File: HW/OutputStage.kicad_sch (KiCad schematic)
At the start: 10 parts, among them U1 DRV8244S-Q1, U2 DRV8244S-Q1

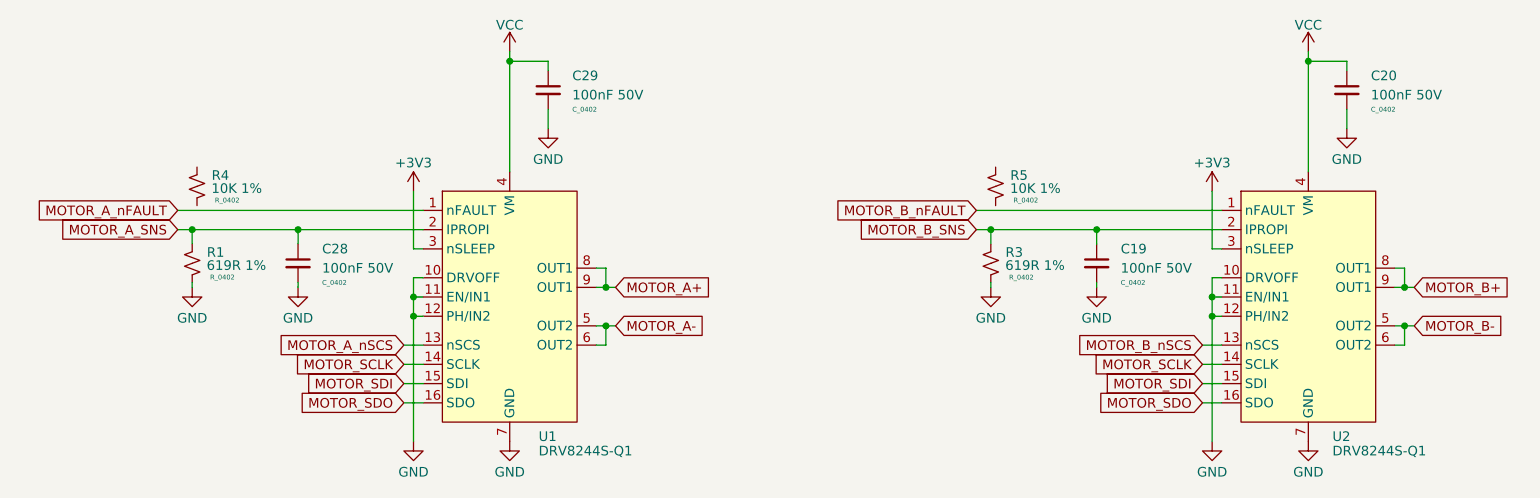
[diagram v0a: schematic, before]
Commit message: WIP - Layout XT30/PCB Finger Positions
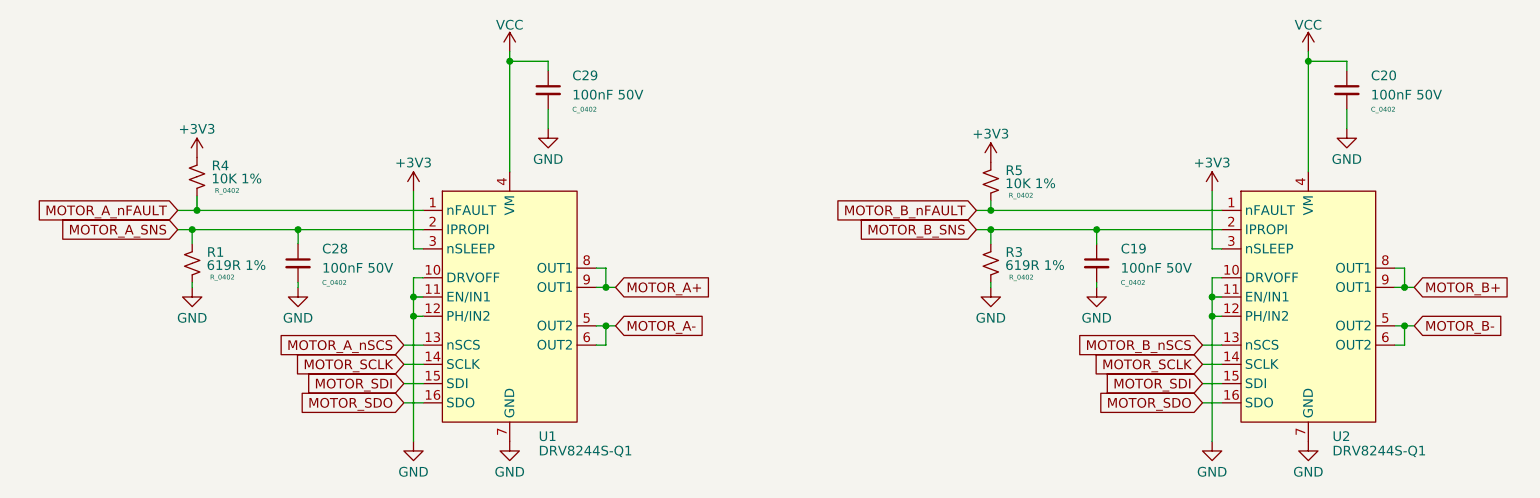
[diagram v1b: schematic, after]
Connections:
- net +3V3: now also R4.1, R5.1
- net MOTOR_A_nFAULT: now also R4.2
- net MOTOR_B_nFAULT: now also R5.2
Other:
- title: WEKA ESC - 20A -> KAKAPO ESC - 20A
- moved on the sheet: R4, R5

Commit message: WIP - Layout Motor Drivers + Buck Circuit
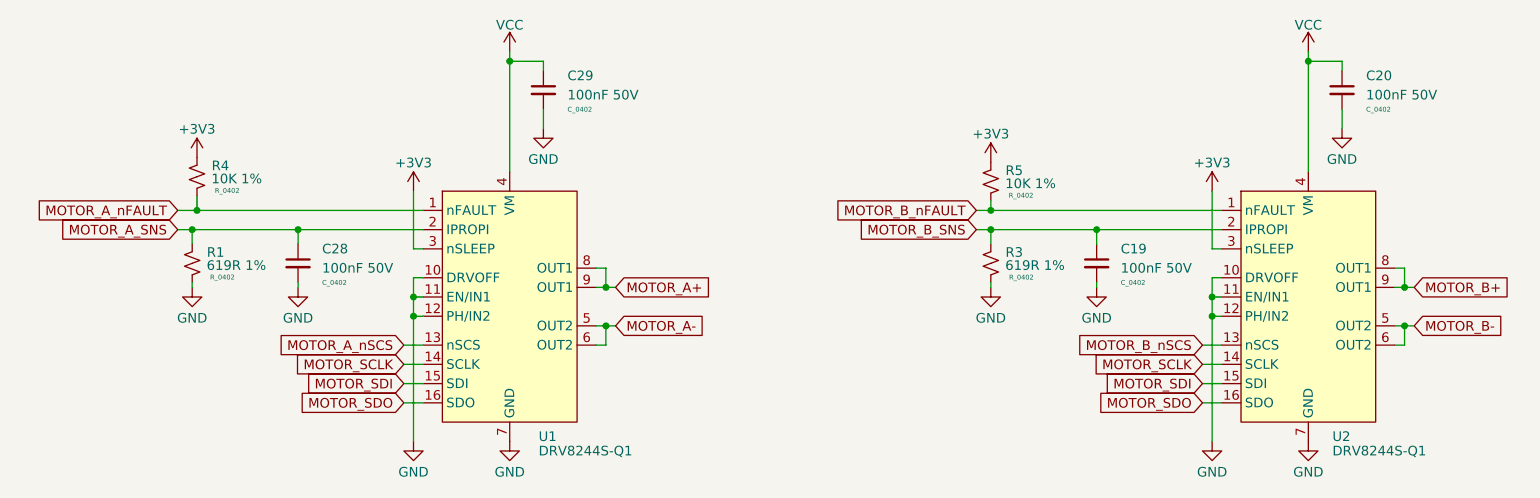
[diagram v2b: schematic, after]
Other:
- moved on the sheet: C20, C29
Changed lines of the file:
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@@
+    (stroke (width 0) (type default))
+  )
+  (wire (pts (xy 109.855 69.85) (xy 114.3 69.85))
     (stroke (width 0) (type default))
   )
@@
     (stroke (width 0) (type default))
   )
-  (wire (pts (xy 114.935 71.12) (xy 114.935 69.85))
+  (wire (pts (xy 114.3 71.12) (xy 114.3 69.85))
     (stroke (width 0) (type default))
   )
@@
     (stroke (width 0) (type default))
   )
-  (wire (pts (xy 220.345 71.12) (xy 220.345 69.85))
+  (wire (pts (xy 219.71 71.12) (xy 219.71 69.85))
     (stroke (width 0) (type default))
   )
@@
     (stroke (width 0) (type default))
   )
-  (wire (pts (xy 109.855 69.85) (xy 114.935 69.85))
-    (stroke (width 0) (type default))
-  )
   (wire (pts (xy 98.425 98.425) (xy 97.155 98.425))
     (stroke (width 0) (type default))
@@
     (stroke (width 0) (type default))
   )
+  (wire (pts (xy 219.71 76.2) (xy 219.71 78.74))
+    (stroke (width 0) (type default))
+  )
   (wire (pts (xy 109.855 69.85) (xy 109.855 84.455))
     (stroke (width 0) (type default))
@@
     (stroke (width 0) (type default))
   )
-  (wire (pts (xy 220.345 76.2) (xy 220.345 78.74))
-    (stroke (width 0) (type default))
-  )
   (wire (pts (xy 67.945 99.695) (xy 67.945 99.06))
     (stroke (width 0) (type default))
@@
     (stroke (width 0) (type default))
   )
-  (wire (pts (xy 114.935 76.2) (xy 114.935 78.74))
+  (wire (pts (xy 114.3 76.2) (xy 114.3 78.74))
     (stroke (width 0) (type default))
   )
@@
     (stroke (width 0) (type default))
   )
-  (wire (pts (xy 215.265 69.85) (xy 220.345 69.85))
+  (wire (pts (xy 215.265 69.85) (xy 219.71 69.85))
     (stroke (width 0) (type default))
   )
@@
     )
   )
-  (symbol (lib_id "power:GND") (at 114.935 78.74 0) (unit 1)
+  (symbol (lib_id "power:GND") (at 114.3 78.74 0) (unit 1)
     (in_bom yes) (on_board yes) (dnp no)
-    (property "Reference" "#PWR026" (at 114.935 85.09 0)
-      (effects (font (size 1.27 1.27)) hide)
-    )
-    (property "Value" "GND" (at 114.935 82.804 0)
+    (property "Reference" "#PWR026" (at 114.3 85.09 0)
+      (effects (font (size 1.27 1.27)) hide)
+    )
+    (property "Value" "GND" (at 114.3 82.804 0)
       (effects (font (size 1.27 1.27)))
     )
-    (property "Footprint" "" (at 114.935 78.74 0)
-      (effects (font (size 1.27 1.27)) hide)
-    )
-    (property "Datasheet" "" (at 114.935 78.74 0)
+    (property "Footprint" "" (at 114.3 78.74 0)
+      (effects (font (size 1.27 1.27)) hide)
+    )
+    (property "Datasheet" "" (at 114.3 78.74 0)
       (effects (font (size 1.27 1.27)) hide)
     )
@@
     )
   )
-  (symbol (lib_id "power:GND") (at 220.345 78.74 0) (unit 1)
+  (symbol (lib_id "power:GND") (at 219.71 78.74 0) (unit 1)
     (in_bom yes) (on_board yes) (dnp no)
-    (property "Reference" "#PWR028" (at 220.345 85.09 0)
-      (effects (font (size 1.27 1.27)) hide)
-    )
-    (property "Value" "GND" (at 220.345 82.804 0)
+    (property "Reference" "#PWR028" (at 219.71 85.09 0)
+      (effects (font (size 1.27 1.27)) hide)
+    )
+    (property "Value" "GND" (at 219.71 82.804 0)
       (effects (font (size 1.27 1.27)))
     )
-    (property "Footprint" "" (at 220.345 78.74 0)
-      (effects (font (size 1.27 1.27)) hide)
-    )
-    (property "Datasheet" "" (at 220.345 78.74 0)
+    (property "Footprint" "" (at 219.71 78.74 0)
+      (effects (font (size 1.27 1.27)) hide)
+    )
+    (property "Datasheet" "" (at 219.71 78.74 0)
       (effects (font (size 1.27 1.27)) hide)
     )
@@
     )
   )
-  (symbol (lib_id "C_Capacitor:C_0402") (at 114.935 73.66 0) (unit 1)
+  (symbol (lib_id "C_Capacitor:C_0402") (at 114.3 73.66 0) (unit 1)
     (in_bom yes) (on_board yes) (dnp no) (fields_autoplaced)
-    (property "Reference" "C29" (at 118.11 71.7613 0)
+    (property "Reference" "C29" (at 117.475 71.7613 0)
       (effects (font (size 1.27 1.27)) (justify left))
     )
-    (property "Value" "100nF 50V" (at 118.11 74.3013 0)
+    (property "Value" "100nF 50V" (at 117.475 74.3013 0)
       (effects (font (size 1.27 1.27)) (justify left))
     )
-    (property "Footprint" "C_Capacitor:C_0402" (at 111.76 73.66 90)
-      (effects (font (size 1.27 1.27)) hide)
-    )
-    (property "Datasheet" "" (at 117.475 71.12 0)
-      (effects (font (size 1.27 1.27)) hide)
-    )
-    (property "Size" "C_0402" (at 118.11 76.2063 0)
+    (property "Footprint" "C_Capacitor:C_0402" (at 111.125 73.66 90)
+      (effects (font (size 1.27 1.27)) hide)
+    )
+    (property "Datasheet" "" (at 116.84 71.12 0)
+      (effects (font (size 1.27 1.27)) hide)
+    )
+    (property "Size" "C_0402" (at 117.475 76.2063 0)
       (effects (font (size 0.635 0.635)) (justify left))
     )
-    (property "LCSC Part" "C105882" (at 114.935 73.66 0)
+    (property "LCSC Part" "C105882" (at 114.3 73.66 0)
       (effects (font (size 1.27 1.27)) hide)
     )
@@
     )
   )
-  (symbol (lib_id "C_Capacitor:C_0402") (at 220.345 73.66 0) (unit 1)
+  (symbol (lib_id "C_Capacitor:C_0402") (at 219.71 73.66 0) (unit 1)
     (in_bom yes) (on_board yes) (dnp no) (fields_autoplaced)
-    (property "Reference" "C20" (at 223.52 71.7613 0)
+    (property "Reference" "C20" (at 222.885 71.7613 0)
       (effects (font (size 1.27 1.27)) (justify left))
     )
-    (property "Value" "100nF 50V" (at 223.52 74.3013 0)
+    (property "Value" "100nF 50V" (at 222.885 74.3013 0)
       (effects (font (size 1.27 1.27)) (justify left))
     )
-    (property "Footprint" "C_Capacitor:C_0402" (at 217.17 73.66 90)
-      (effects (font (size 1.27 1.27)) hide)
-    )
-    (property "Datasheet" "" (at 222.885 71.12 0)
-      (effects (font (size 1.27 1.27)) hide)
-    )
-    (property "Size" "C_0402" (at 223.52 76.2063 0)
+    (property "Footprint" "C_Capacitor:C_0402" (at 216.535 73.66 90)
+      (effects (font (size 1.27 1.27)) hide)
+    )
+    (property "Datasheet" "" (at 222.25 71.12 0)
+      (effects (font (size 1.27 1.27)) hide)
+    )
+    (property "Size" "C_0402" (at 222.885 76.2063 0)
       (effects (font (size 0.635 0.635)) (justify left))
     )
-    (property "LCSC Part" "C105882" (at 220.345 73.66 0)
-      (effects (font (size 1.27 1.27)) hide)
-    )
+    (property "LCSC Part" "C105882" (at 219.71 73.66 0)
+      (effects (font (size 1.27 1.27)) hide)
+    )

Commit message: Finish Tracking and Release For MFG
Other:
- title: KAKAPO ESC - 20A -> KAKAPO - 20A
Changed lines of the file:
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@@
   (paper "A4")
   (title_block
-    (title "KAKAPO ESC - 20A")
-    (date "2024-03-10")
-    (rev "v1.0")
+    (title "KAKAPO - 20A")
+    (date "2024-04-27")
+    (rev "v0.1")
     (company "CB-TECHNOLOGY")
   )
@@
     (pin "1")
     (instances
-      (project "KAKAPO_ESC-20A"
+      (project "KAKAPO-20A"
         (path "/e63e39d7-6ac0-4ffd-8aa3-1841a4541b55/d37f63d1-7ddf-4854-b3a4-c1738f7e36ae"
           (reference "#PWR039") (unit 1)
@@
     (pin "2")
     (instances
-      (project "KAKAPO_ESC-20A"
+      (project "KAKAPO-20A"
         (path "/e63e39d7-6ac0-4ffd-8aa3-1841a4541b55/d37f63d1-7ddf-4854-b3a4-c1738f7e36ae"
           (reference "R5") (unit 1)
@@
     (pin "1")
     (instances
-      (project "KAKAPO_ESC-20A"
+      (project "KAKAPO-20A"
         (path "/e63e39d7-6ac0-4ffd-8aa3-1841a4541b55/d37f63d1-7ddf-4854-b3a4-c1738f7e36ae"
           (reference "#PWR044") (unit 1)
@@
     (pin "1")
     (instances
-      (project "KAKAPO_ESC-20A"
+      (project "KAKAPO-20A"
         (path "/e63e39d7-6ac0-4ffd-8aa3-1841a4541b55/d37f63d1-7ddf-4854-b3a4-c1738f7e36ae"
           (reference "#PWR017") (unit 1)
@@
     (pin "9")
     (instances
-      (project "KAKAPO_ESC-20A"
+      (project "KAKAPO-20A"
         (path "/e63e39d7-6ac0-4ffd-8aa3-1841a4541b55/d37f63d1-7ddf-4854-b3a4-c1738f7e36ae"
           (reference "U1") (unit 1)
@@
     (pin "1")
     (instances
-      (project "KAKAPO_ESC-20A"
+      (project "KAKAPO-20A"
         (path "/e63e39d7-6ac0-4ffd-8aa3-1841a4541b55/d37f63d1-7ddf-4854-b3a4-c1738f7e36ae"
           (reference "#PWR026") (unit 1)
@@
     (pin "1")
     (instances
-      (project "KAKAPO_ESC-20A"
+      (project "KAKAPO-20A"
         (path "/e63e39d7-6ac0-4ffd-8aa3-1841a4541b55/d37f63d1-7ddf-4854-b3a4-c1738f7e36ae"
           (reference "#PWR015") (unit 1)
@@
     (pin "2")
     (instances
-      (project "KAKAPO_ESC-20A"
+      (project "KAKAPO-20A"
         (path "/e63e39d7-6ac0-4ffd-8aa3-1841a4541b55/d37f63d1-7ddf-4854-b3a4-c1738f7e36ae"
           (reference "C28") (unit 1)
@@
     (pin "2")
     (instances
-      (project "KAKAPO_ESC-20A"
+      (project "KAKAPO-20A"
         (path "/e63e39d7-6ac0-4ffd-8aa3-1841a4541b55/d37f63d1-7ddf-4854-b3a4-c1738f7e36ae"
           (reference "R3") (unit 1)
@@
     (pin "2")
     (instances
-      (project "KAKAPO_ESC-20A"
+      (project "KAKAPO-20A"
         (path "/e63e39d7-6ac0-4ffd-8aa3-1841a4541b55/d37f63d1-7ddf-4854-b3a4-c1738f7e36ae"
           (reference "R1") (unit 1)
@@
     (pin "2")
     (instances
-      (project "KAKAPO_ESC-20A"
+      (project "KAKAPO-20A"
         (path "/e63e39d7-6ac0-4ffd-8aa3-1841a4541b55/d37f63d1-7ddf-4854-b3a4-c1738f7e36ae"
           (reference "R4") (unit 1)
@@
     (pin "1")
     (instances
-      (project "KAKAPO_ESC-20A"
+      (project "KAKAPO-20A"
         (path "/e63e39d7-6ac0-4ffd-8aa3-1841a4541b55/d37f63d1-7ddf-4854-b3a4-c1738f7e36ae"
           (reference "#PWR028") (unit 1)
@@
     (pin "1")
     (instances
-      (project "KAKAPO_ESC-20A"
+      (project "KAKAPO-20A"
         (path "/e63e39d7-6ac0-4ffd-8aa3-1841a4541b55/d37f63d1-7ddf-4854-b3a4-c1738f7e36ae"
           (reference "#PWR038") (unit 1)
@@
     (pin "1")
     (instances
-      (project "KAKAPO_ESC-20A"
+      (project "KAKAPO-20A"
         (path "/e63e39d7-6ac0-4ffd-8aa3-1841a4541b55/d37f63d1-7ddf-4854-b3a4-c1738f7e36ae"
           (reference "#PWR016") (unit 1)
@@
     (pin "1")
     (instances
-      (project "KAKAPO_ESC-20A"
+      (project "KAKAPO-20A"
         (path "/e63e39d7-6ac0-4ffd-8aa3-1841a4541b55/d37f63d1-7ddf-4854-b3a4-c1738f7e36ae"
           (reference "#PWR030") (unit 1)
@@
     (pin "2")
     (instances
-      (project "KAKAPO_ESC-20A"
+      (project "KAKAPO-20A"
         (path "/e63e39d7-6ac0-4ffd-8aa3-1841a4541b55/d37f63d1-7ddf-4854-b3a4-c1738f7e36ae"
           (reference "C29") (unit 1)
@@
     (pin "1")
     (instances
-      (project "KAKAPO_ESC-20A"
+      (project "KAKAPO-20A"
         (path "/e63e39d7-6ac0-4ffd-8aa3-1841a4541b55/d37f63d1-7ddf-4854-b3a4-c1738f7e36ae"
           (reference "#PWR019") (unit 1)
@@
     (pin "1")
     (instances
-      (project "KAKAPO_ESC-20A"
+      (project "KAKAPO-20A"
         (path "/e63e39d7-6ac0-4ffd-8aa3-1841a4541b55/d37f63d1-7ddf-4854-b3a4-c1738f7e36ae"
           (reference "#PWR018") (unit 1)
@@
     (pin "9")
     (instances
-      (project "KAKAPO_ESC-20A"
+      (project "KAKAPO-20A"
         (path "/e63e39d7-6ac0-4ffd-8aa3-1841a4541b55/d37f63d1-7ddf-4854-b3a4-c1738f7e36ae"
           (reference "U2") (unit 1)
@@
     (pin "1")
     (instances
-      (project "KAKAPO_ESC-20A"
+      (project "KAKAPO-20A"
         (path "/e63e39d7-6ac0-4ffd-8aa3-1841a4541b55/d37f63d1-7ddf-4854-b3a4-c1738f7e36ae"
           (reference "#PWR024") (unit 1)
@@
     (pin "2")
     (instances
-      (project "KAKAPO_ESC-20A"
+      (project "KAKAPO-20A"
         (path "/e63e39d7-6ac0-4ffd-8aa3-1841a4541b55/d37f63d1-7ddf-4854-b3a4-c1738f7e36ae"
           (reference "C19") (unit 1)
@@
     (pin "1")
     (instances
-      (project "KAKAPO_ESC-20A"
+      (project "KAKAPO-20A"
         (path "/e63e39d7-6ac0-4ffd-8aa3-1841a4541b55/d37f63d1-7ddf-4854-b3a4-c1738f7e36ae"
           (reference "#PWR022") (unit 1)
@@
     (pin "1")
     (instances
-      (project "KAKAPO_ESC-20A"
+      (project "KAKAPO-20A"
         (path "/e63e39d7-6ac0-4ffd-8aa3-1841a4541b55/d37f63d1-7ddf-4854-b3a4-c1738f7e36ae"
           (reference "#PWR011") (unit 1)
@@
     (pin "2")
     (instances
-      (project "KAKAPO_ESC-20A"
+      (project "KAKAPO-20A"
         (path "/e63e39d7-6ac0-4ffd-8aa3-1841a4541b55/d37f63d1-7ddf-4854-b3a4-c1738f7e36ae"
           (reference "C20") (unit 1)
@@
     (pin "1")
     (instances
-      (project "KAKAPO_ESC-20A"
+      (project "KAKAPO-20A"
         (path "/e63e39d7-6ac0-4ffd-8aa3-1841a4541b55/d37f63d1-7ddf-4854-b3a4-c1738f7e36ae"
           (reference "#PWR023") (unit 1)
@@
     (pin "1")
     (instances
-      (project "KAKAPO_ESC-20A"
+      (project "KAKAPO-20A"
         (path "/e63e39d7-6ac0-4ffd-8aa3-1841a4541b55/d37f63d1-7ddf-4854-b3a4-c1738f7e36ae"
           (reference "#PWR043") (unit 1)

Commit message: Create v1.0 Fixed From v0.2 HW
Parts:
- R1, R3: LCSC Part C309549 -> C5121525
- R4, R5: LCSC Part C309549 -> C60490
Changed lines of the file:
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@@
       (effects (font (size 1.27 1.27)) hide)
     )
-    (property "LCSC Part" "C309549" (at 173.355 85.725 0)
+    (property "LCSC Part" "C60490" (at 173.355 85.725 0)
       (effects (font (size 1.27 1.27)) hide)
     )
@@
       (effects (font (size 1.27 1.27)) hide)
     )
-    (property "LCSC Part" "C309549" (at 173.355 96.52 0)
+    (property "LCSC Part" "C5121525" (at 173.355 96.52 0)
       (effects (font (size 1.27 1.27)) hide)
     )
@@
       (effects (font (size 1.27 1.27)) hide)
     )
-    (property "LCSC Part" "C309549" (at 67.945 96.52 0)
+    (property "LCSC Part" "C5121525" (at 67.945 96.52 0)
       (effects (font (size 1.27 1.27)) hide)
     )
@@
       (effects (font (size 1.27 1.27)) hide)
     )
-    (property "LCSC Part" "C309549" (at 68.58 85.09 0)
-      (effects (font (size 1.27 1.27)) hide)
-    )
+    (property "LCSC Part" "C60490" (at 68.58 85.09 0)
+      (effects (font (size 1.27 1.27)) hide)
+    )
